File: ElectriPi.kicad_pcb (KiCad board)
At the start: 2 copper layers, 65 x 56 mm, 44 parts, among them J1 2444, J2 JST XH 01x02, J3 JST XH 01x02, J6 Raspberry_Pi_2_3, J8 JST XH 01x02, Q1 30V 4A 44mΩ, Q2 50nA 150V 200mW 200mA, Q3 30V 4A 44mΩ, U1 XL4015

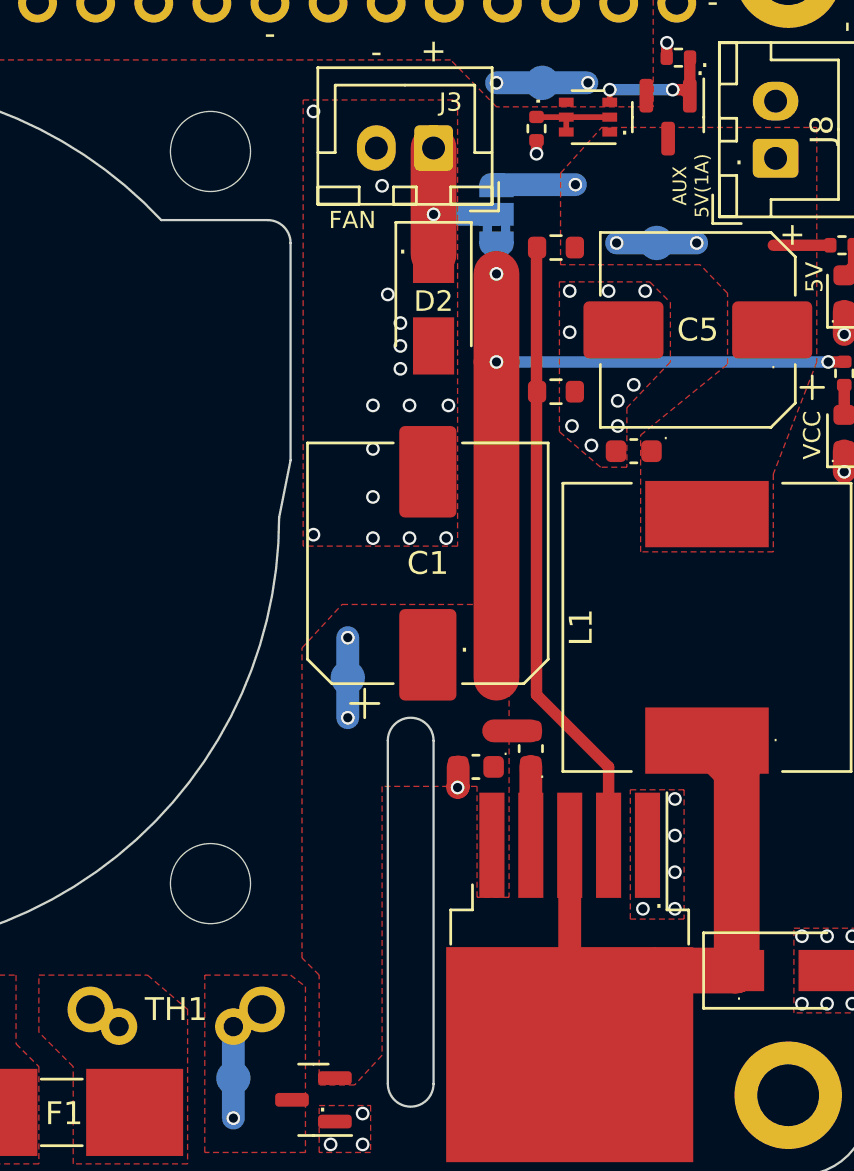
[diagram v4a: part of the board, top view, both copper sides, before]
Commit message: Some small adjustment to silkscreen
rotated TP on b.silk to match other text
hid reference text for pin socket
hid reference text for ICL
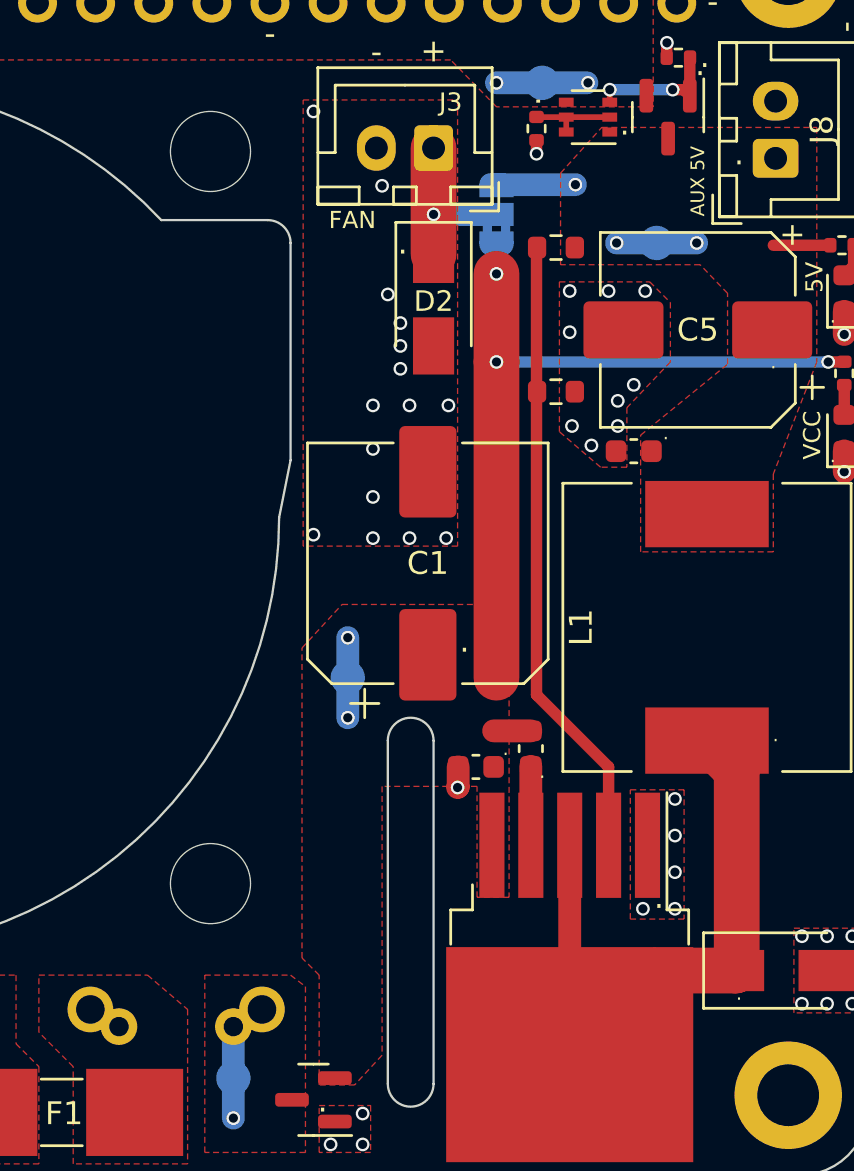
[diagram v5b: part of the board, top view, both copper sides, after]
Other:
- board text added: "AUX 5V"
- board text removed: "AUX 5V(1A)"
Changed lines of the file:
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@@
     (property "Sheetname" "")
     (attr through_hole)
-    (fp_text reference "TH1" (at 3.75 0 unlocked) (layer "F.SilkS")
+    (fp_text reference "TH1" (at 3.75 0 unlocked) (layer "User.2")
       (effects (font (size 1 1) (thickness 0.15)))
     )
@@
     (property "Sheetname" "")
     (attr exclude_from_pos_files)
-    (fp_text reference "TP5" (at -2 -1.5) (layer "B.SilkS")
+    (fp_text reference "TP5" (at -1.5 -2.1 270 unlocked) (layer "B.SilkS")
       (effects (font (size 1 1) (thickness 0.15)) (justify mirror))
     )
@@
     (property "exclude_from_bom" "")
     (attr through_hole exclude_from_bom)
-    (fp_text reference "J6" (at 2.28 0.02 -90 unlocked) (layer "B.SilkS")
+    (fp_text reference "J6" (at 2.28 0.02 -90 unlocked) (layer "User.2")
       (effects (font (size 1 1) (thickness 0.15)) (justify mirror))
     )
@@
     (property "exclude_from_bom" "")
     (attr exclude_from_pos_files exclude_from_bom)
-    (fp_text reference "JP1" (at 2.45 2.2 270 unlocked) (layer "B.SilkS")
+    (fp_text reference "JP1" (at 2.45 2.2 270 unlocked) (layer "User.2")
       (effects (font (size 1 1) (thickness 0.15)) (justify mirror))
     )
@@
     (property "Sheetname" "")
     (attr exclude_from_pos_files)
-    (fp_text reference "TP4" (at -3 0) (layer "B.SilkS")
+    (fp_text reference "TP4" (at -1.5 2 270 unlocked) (layer "B.SilkS")
       (effects (font (size 1 1) (thickness 0.15)) (justify mirror))
     )
@@
     (property "Sheetname" "")
     (attr exclude_from_pos_files)
-    (fp_text reference "TP1" (at 0 1.648) (layer "B.SilkS")
+    (fp_text reference "TP1" (at -0.9 2.4 270 unlocked) (layer "B.SilkS")
       (effects (font (size 1 1) (thickness 0.15)) (justify mirror))
     )
@@
     (property "Sheetname" "")
     (attr exclude_from_pos_files)
-    (fp_text reference "TP2" (at 0 1.648) (layer "B.SilkS")
+    (fp_text reference "TP2" (at -1.7 -2.3 270 unlocked) (layer "B.SilkS")
       (effects (font (size 1 1) (thickness 0.15)) (justify mirror))
     )
@@
     (property "Sheetname" "")
     (attr exclude_from_pos_files)
-    (fp_text reference "TP3" (at 3 0) (layer "B.SilkS")
+    (fp_text reference "TP3" (at 2.1 -1.5 270 unlocked) (layer "B.SilkS")
       (effects (font (size 1 1) (thickness 0.15)) (justify mirror))
     )
@@
     (effects (font (size 0.75 0.75) (thickness 0.15)))
   )
-  (gr_text "AUX\n5V(1A)" (at 142.5 66 90) (layer "F.SilkS")
+  (gr_text "AUX 5V" (at 142.8 65.8 90) (layer "F.SilkS")
     (effects (font (size 0.6 0.6) (thickness 0.125)))
   )

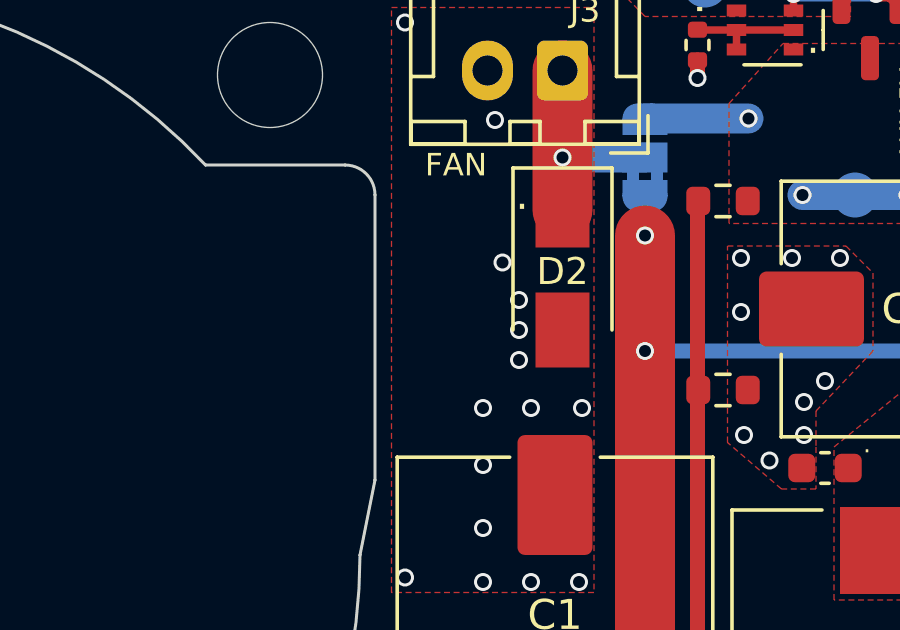
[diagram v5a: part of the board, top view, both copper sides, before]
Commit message: adding GND test point
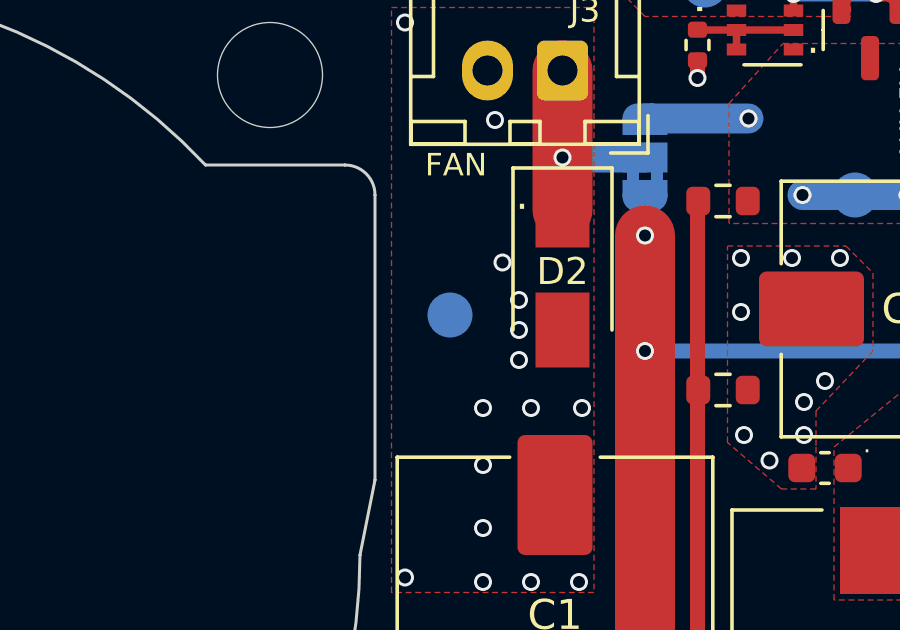
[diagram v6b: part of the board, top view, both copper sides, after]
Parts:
- added TP6: TestPoint, TestPoint:TestPoint_Pad_D1.5mm, B.Cu at (127.5, 72.5)
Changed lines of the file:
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@@
     (descr "JST XH series connector, B2B-XH-A (http://www.jst-mfg.com/product/pdf/eng/eXH.pdf), generated with kicad-footprint-generator")
     (tags "connector JST XH vertical")
+    (property "LCSC" "C492456")
     (property "PCBway" "")
     (property "Sheetfile" "ElectriPi.kicad_sch")
@@
     (descr "JST XH series connector, B2B-XH-A (http://www.jst-mfg.com/product/pdf/eng/eXH.pdf), generated with kicad-footprint-generator")
     (tags "connector JST XH vertical")
+    (property "LCSC" "C492456")
     (property "Sheetfile" "ElectriPi.kicad_sch")
     (property "Sheetname" "")
@@
     (descr "Terminal Block 4Ucon ItemNo. 19963, 2 pins, pitch 3.5mm, size 7.7x7mm^2, drill diamater 1.2mm, pad diameter 2.4mm, see http://www.4uconnector.com/online/object/4udrawing/19963.pdf, script-generated using https://github.com/pointhi/kicad-footprint-generator/scripts/TerminalBlock_4Ucon")
     (tags "THT Terminal Block 4Ucon ItemNo. 19963 pitch 3.5mm size 7.7x7mm^2 drill 1.2mm pad 2.4mm")
-    (property "LCSC" "")
+    (property "LCSC" "C123214")
     (property "PCBway" "")
     (property "Sheetfile" "ElectriPi.kicad_sch")
@@
     (descr "JST XH series connector, B2B-XH-A (http://www.jst-mfg.com/product/pdf/eng/eXH.pdf), generated with kicad-footprint-generator")
     (tags "connector JST XH vertical")
-    (property "LCSC" "")
+    (property "LCSC" "C492456")
     (property "PCBway" "")
     (property "Sheetfile" "ElectriPi.kicad_sch")
@@
   (footprint "Inrush_Limiter:5_OR_7pt5_PITCH_ICL" (layer "F.Cu")
     (at 116.25 102)
+    (property "Mouser" " 871-B57238S0709M000")
     (property "Sheetfile" "ElectriPi.kicad_sch")
     (property "Sheetname" "")
@@
   )
   (footprint "TestPoint:TestPoint_Pad_D1.5mm" (layer "B.Cu")
+    (at 127.5 72.5 180)
+    (descr "SMD pad as test Point, diameter 1.5mm")
+    (tags "test point SMD pad")
+    (property "Sheetfile" "ElectriPi.kicad_sch")
+    (property "Sheetname" "")
+    (attr exclude_from_pos_files)
+    (fp_text reference "TP6" (at 0 1.648) (layer "B.SilkS")
+      (effects (font (size 1 1) (thickness 0.15)) (justify mirror))
+    )
+    (fp_text value "TestPoint" (at 0 -1.75) (layer "B.Fab")
+      (effects (font (size 1 1) (thickness 0.15)) (justify mirror))
+    )
+    (fp_text user "${REFERENCE}" (at 0 1.65) (layer "B.Fab")
+      (effects (font (size 1 1) (thickness 0.15)) (justify mirror))
+    )
+    (fp_circle (center 0 0) (end 0 -0.95) (layer "B.SilkS") (width 0.12) (fill none))
+    (fp_circle (center 0 0) (end 1.25 0) (layer "B.CrtYd") (width 0.05) (fill none))
+    (pad "1" smd circle (at 0 0 180) (size 1.5 1.5) (layers "B.Cu" "B.Mask")
+      (net 2 "GND") (pinfunction "1") (pintype "passive"))
+  )
+  (footprint "TestPoint:TestPoint_Pad_D1.5mm" (layer "B.Cu")

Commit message: Back Silkscreen Adjustments
Test point reference labels now hidden.
Adjusted credentials to match ElectriPi Mini
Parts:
- removed the G*** at (143.7, 85.0)
- added G***: LOGO, LOGO, B.Cu at (141.9, 84.5)
- moved G*** 3.27 mm to (138.5, 91.5)
- moved G*** 1.91 mm to (135.1, 81.0)
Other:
- board text added: "Designed by Sreenivas Eadara"
- board text added: "Manufactured by LDO Motors"
- board text removed: "Designed by Sreenivas Eadara, Produced by LDO Motors"
